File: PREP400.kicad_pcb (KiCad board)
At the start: 4 copper layers, 260.2 x 144.2 mm, 484 parts, among them IC1 SSC, IC10 L293DD, IC11 L6472, IC12 L6472, IC13 L6472, IC14 L6472, IC2 SSC, IC3 SSC, IC4 SSC, IC5 L6472, IC6 L6472, IC7 L6472, IC8 L6472, IC9 L293DD, J1 MTA04-156, J10 MTA02-100, J11 MTA02-100, J12 MTA02-100, J13 MTA02-100, J14 MTA03-100, J15 MTA03-100, J16 MTA03-100, J17 MTA03-100, J18 MTA04-100, J19 MTA04-100, J2 MTA02-100, J20 MTA04-100, J21 MTA04-100, J22 MTA05-100, J23 MTA05-100, J24 MTA05-100, J25 MTA05-100, J26 MTA04-100, J27 MTA04-100, J28 MTA04-100, J29 MTA04-100, J3 MTA02-100, J4 MTA03-100, J5 MTA03-100, J6 MTA03-100, J7 MTA03-100, J8 MTA02-100, J9 MTA02-100, P1 CONN_EXP2, Q1 FQT13N06L, Q2 FQT13N06L, Q3 FQT13N06L, Q4 FQT13N06L, Q5 FQT13N06L, Q6 FQT13N06L, Q7 FQT13N06L, U1 FRDM-KL25Z

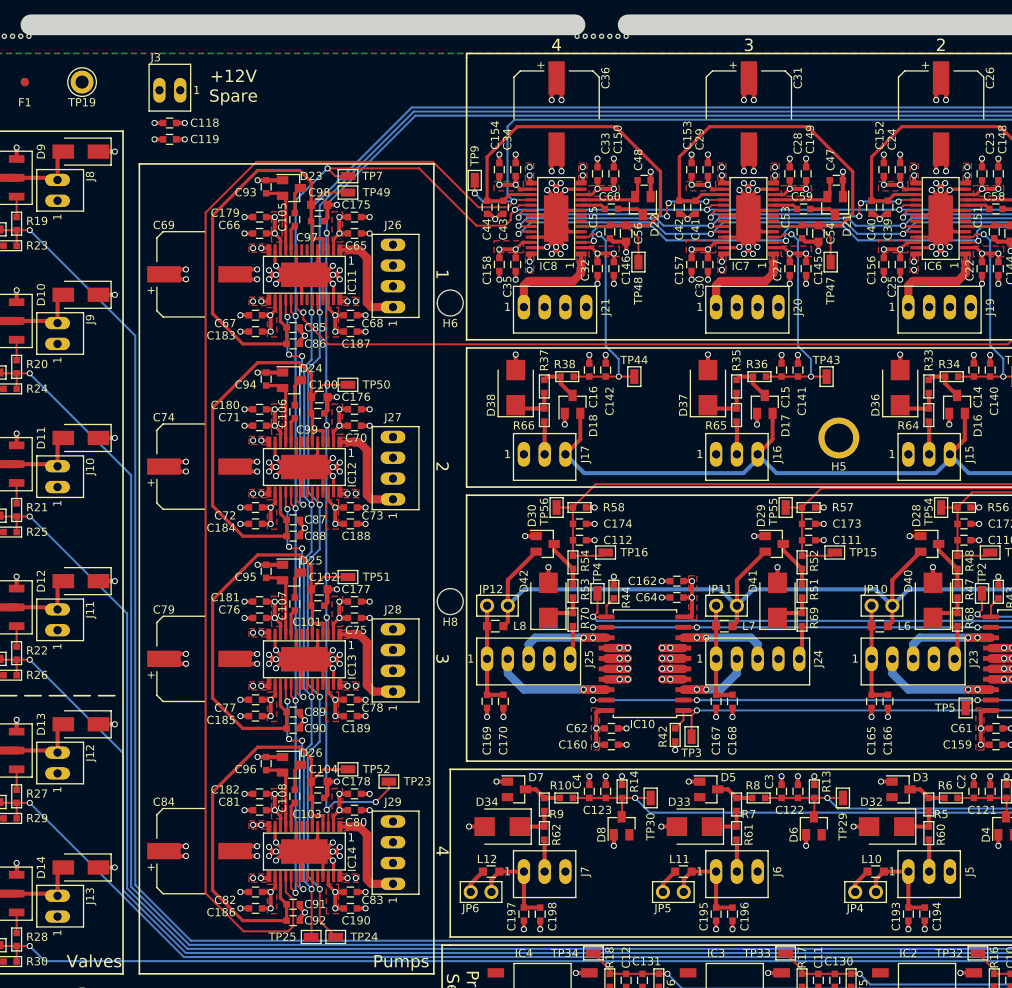
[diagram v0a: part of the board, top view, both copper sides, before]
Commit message: Added fab drawing for assembly
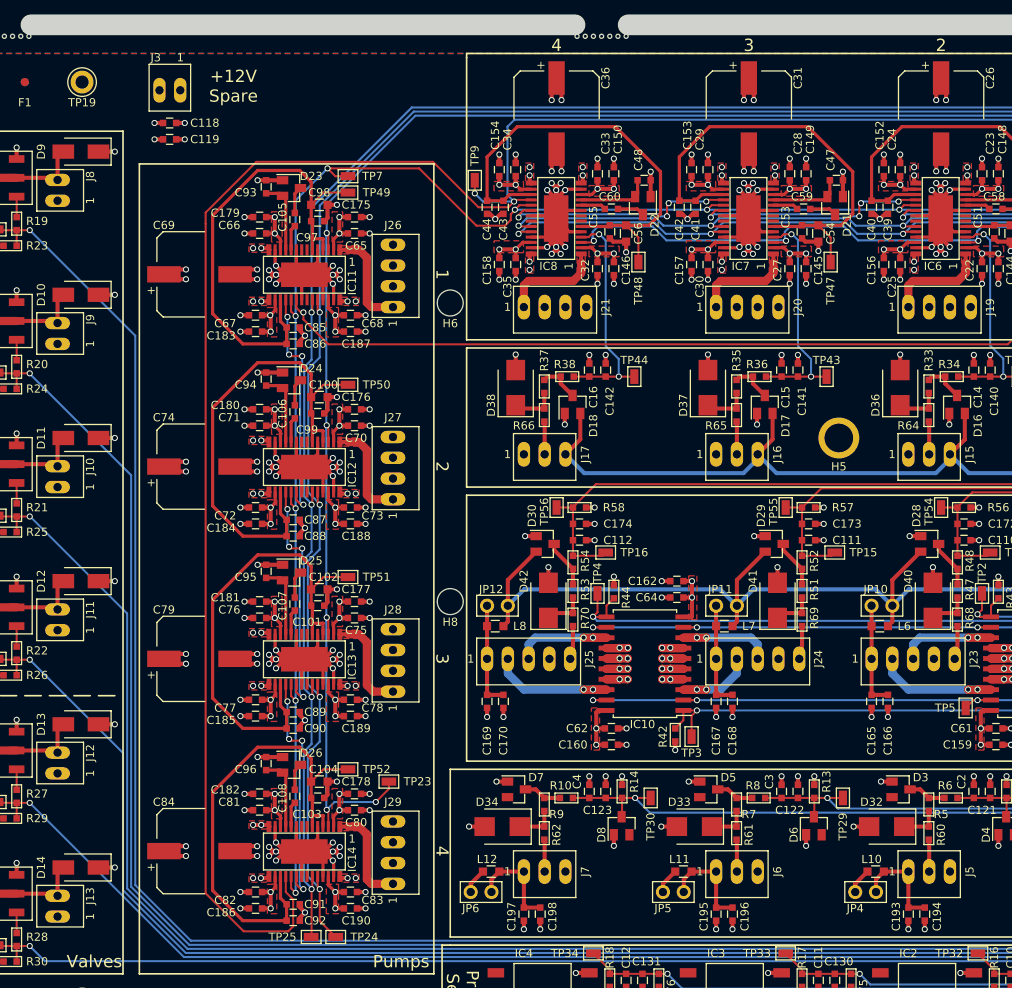
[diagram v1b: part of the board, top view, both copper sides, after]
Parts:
- TP19, TP20, TP21, TP22: footprint Measurement_Points:Test_Point_Keystone_5005-5009_Compact -> probes:Test_Point_Keystone_5005-5009_Compact

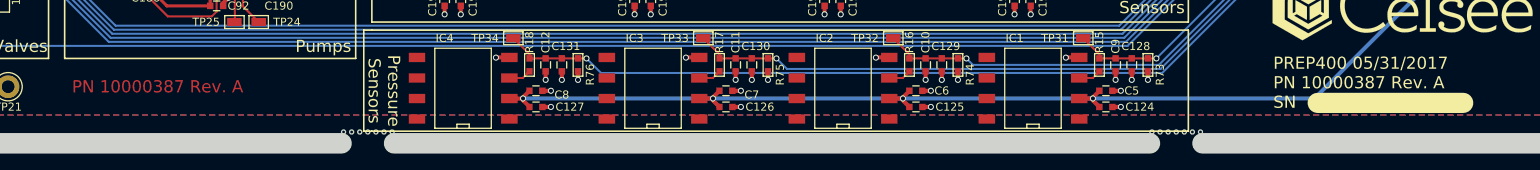
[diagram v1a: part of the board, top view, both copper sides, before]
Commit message: Added part numbers
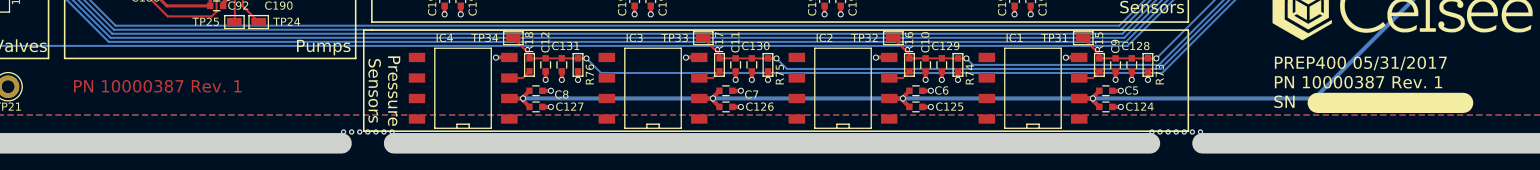
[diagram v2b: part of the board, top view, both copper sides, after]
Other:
- board text added: "PN 10000387 Rev. 1"
- board text added: "PREP400 05/31/2017 PN 10000387 Rev. 1 SN"
- board text removed: "PN 10000387 Rev. A"
- board text removed: "PREP400 05/31/2017 PN 10000387 Rev. A SN"
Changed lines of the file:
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@@
   )
   (layers
-    (0 F.Cu signal hide)
+    (0 F.Cu signal)
     (1 In1.Cu mixed hide)
     (2 In2.Cu mixed hide)
@@
     (visible_elements 7FFCF77F)
     (pcbplotparams
-      (layerselection 0x20000_7ffffff8)
-      (usegerberextensions false)
+      (layerselection 0x30000_7ffffff8)
+      (usegerberextensions true)
       (usegerberattributes false)
       (usegerberadvancedattributes false)
@@
       (xy 13.636625 -3.81)) (layer F.SilkS) (width 0.01))
   )
-  (gr_text "PN 10000387 Rev. A" (at 65.4 148.05) (layer F.Cu)
+  (gr_text "PN 10000387 Rev. 1" (at 65.4 148.05) (layer F.Cu)
     (effects (font (size 1.5 1.5) (thickness 0.3)))
   )
@@
   (gr_line (start 93.9 32.55) (end 93.9 67.05) (angle 90) (layer F.SilkS) (width 0.2))
   (gr_line (start 208.9 150.05) (end 226.9 150.05) (angle 90) (layer F.SilkS) (width 2.5))
-  (gr_text "PREP400 05/31/2017\nPN 10000387 Rev. A\nSN \n" (at 203.4 147.55) (layer F.SilkS)
+  (gr_text "PREP400 05/31/2017\nPN 10000387 Rev. 1\nSN \n" (at 203.4 147.55) (layer F.SilkS)
     (effects (font (size 1.5 1.5) (thickness 0.3)) (justify left))
   )

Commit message: Paramit release
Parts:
- G***: footprint logos:CELSEE_LOGO -> logos:CELSEE_LOGO_NEW
- moved C79 48.8 mm to (89.9, 142.1)
- moved D12 48.8 mm to (81.9, 132.6)
- moved D13 48.8 mm to (81.9, 150.1)
- moved J11 48.8 mm to (76.9, 138.6)
- moved J12 48.8 mm to (76.9, 156.1)
- moved Q5 48.8 mm to (71.9, 138.1)
- moved Q6 48.8 mm to (71.9, 155.6)
- moved R22 48.8 mm to (71.9, 140.6)
- moved R26 48.8 mm to (71.9, 144.1)
- moved R27 48.8 mm to (71.9, 158.1)
- moved R29 48.8 mm to (71.9, 161.6)
- moved TP38 48.8 mm to (69.4, 142.1)
- moved TP39 48.8 mm to (69.4, 159.6)
- moved C1 48.8 mm to (212.4, 159.1)
- moved C101 48.8 mm to (107.9, 135.6)
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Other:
- outline, holes or cut-outs redrawn
- board text added: "05/31/2017"
- board text added: "06/07/2018"
- board text added: "1. ASSEMBLE IN ACCORDANCE WITH IPC-A-610, CLASS 2."
- board text added: "1. FABRICATE IN ACCORDANCE WITH IPC-6011 & IPC-6012, CLASS 2."
- board text added: "10/31/2018"
- board text added: "120"
- board text added: "1200"
- board text added: "2. MIN OF 0.001" COPPER IN PLATED HOLE."
- board text added: "2. USE ROHS COMPLIANT PROCESS."
- board text added: "3. MATERIAL:"
- board text added: "3. PLACE EACH PCBA IN ANTI-STATIC BAG."
- board text added: "35"
- board text added: "4. FINISH:"
- board text added: "4. PROTECT IN SHIPPING CONTAINER TO PREVENT DAMAGE UNDER NORMAL TRANSPORT AND HANDLING."
- board text added: "5. CUT CORNER DENOTES PIN 1 OF COMPONENT OR COMPONENT OUTLINE."
- board text added: "5. SOLDER MASK:"
- board text added: "6. SILKSCREEN:"
- board text added: "7"
- board text added: "7. DRILL:"
- board text added: "8. SIZE:"
- board text added: "A"
- board text added: "Approved"
- board text added: "BLUE SOLDERMASK APPLIED BOTH SIDES."
- board text added: "BOARD SIZE W/RAILS IS 10.24" x 5.67"."
- board text added: "Boniface"
- board text added: "Bottom Signal"
- board text added: "Copper"
- board text added: "Date"
- board text added: "Description"
- board text added: "FR4"
- board text added: "Genesis Release"
- board text added: "Genesis V2 Daughter PN 10000387 Rev. 1"
- board text added: "Ground"
- board text added: "HOLE SIZES ARE FINISHED DIAMETERS. HOLE SIZE TOLERANCE: +/- 0.003""
- board text added: "Initial Release"
- board text added: "Layer"
- board text added: "Material"
- board text added: "NOTES:"
- board text added: "Name"
- board text added: "Oz."
- board text added: "Paramit Release"
- board text added: "Pre-Preg"
- board text added: "REVISIONS"
- board text added: "ROHS DIRECTIVE COMPLIANCE REQUIRED. USE FR-4 MATERIAL OR EQUIVALENT. MEET UL 94V-0 FLAMMABILITY RATING. ALL COPPER LAYERS ARE 1.0 OZ. FINAL THICKNESS: 0.062" / 1.6MM FINAL THICKNESS TOLERANCE: 10% FINAL THICKNESS INCLUDES: SOLDER MASK, SILKSCREEN & PLATING."
- board text added: "Rev."
- board text added: "SURFACE FINISH ENIG."
- board text added: "Thickness (um)"
- board text added: "Top Signal"
- board text added: "WHITE NON-CONDUCTIVE PERMANENT INK. SILKSCREEN IS NOT ALLOWED ON PAD."
- board text removed: "PREP400 05/31/2017 PN 10000387 Rev. 1 SN"

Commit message: Address DFM from Paramit
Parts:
- moved TP37 6.50 mm to (75.9, 124.7)
- moved TP38 6.50 mm to (75.9, 142.2)
- moved TP35 6.50 mm to (75.9, 89.5)
- moved TP36 6.50 mm to (75.9, 107.0)
- moved TP39 6.50 mm to (75.9, 159.6)
- moved TP40 6.00 mm to (75.4, 177.1)
- moved L5 1.00 mm to (205.4, 138.1)
- moved L6 1.00 mm to (177.4, 138.1)
- moved L7 1.00 mm to (158.4, 138.1)
- moved L8 1.00 mm to (130.4, 138.1)
- moved C45 0.50 mm to (219.9, 83.0)
- moved C46 0.50 mm to (196.4, 83.0)
- moved C47 0.50 mm to (172.9, 83.0)
- moved C48 0.50 mm to (149.4, 83.0)
- moved C93 0.50 mm to (101.9, 83.5)
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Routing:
- net GND: track 821.0 -> 754.4 mm
- net +12V: track 339.9 -> 335.5 mm
- net /Microcontroller/LAMP: track 63.8 -> 67.3 mm
- net +3V3: track 593.2 -> 591.2 mm
- net Net-(C191-Pad2): track 12.3 -> 14.3 mm
- net Net-(C195-Pad2): track 12.3 -> 14.3 mm
- net Net-(C193-Pad2): track 12.3 -> 14.2 mm
- net Net-(C197-Pad2): track 12.3 -> 14.1 mm
- net Net-(D39-Pad1): track 6.00 -> 7.81 mm
- net /LinearActuator/LIN_OUT3B: track 14.0 -> 12.4 mm
- net /LinearActuator/LIN_OUT1B: track 14.0 -> 12.4 mm
- net /LinearActuator/LIN_OUT4B: track 14.5 -> 12.8 mm
- net /LinearActuator/LIN_OUT2B: track 14.5 -> 12.8 mm
- net /LinearActuator/LIN_OUT3A: track 11.9 -> 10.3 mm
- net /LinearActuator/LIN_OUT1A: track 11.9 -> 10.3 mm
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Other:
- rule pad_to_mask_clearance: 0.2 -> 0.0508
- board text added: "03/29/2019"
- board text added: "9. ROUTING:"
- board text added: "COMPONENTS IC1 - IC4 OVERHANG THE ROUTER PATH. DO NOT ROUTE THIS SECTION."
- board text added: "DFM Updates"
- board text added: "Genesis V2 Daughter PN 10000387 Rev. 2"
- board text added: "PN 10000387 Rev. 2"
- board text removed: "Genesis V2 Daughter PN 10000387 Rev. 1"
- board text removed: "PN 10000387 Rev. 1"
